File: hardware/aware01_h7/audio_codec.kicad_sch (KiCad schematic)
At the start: 6 parts, among them IC2 TLV320AIC3204IRHBR

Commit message: update pcb
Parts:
- added C60: 100n, Capacitor_SMD:C_0603_1608Metric, symbol Device:C
- C38, C40, C41: Manufacturer_Name (none) -> Murata Electronics; Manufacturer_Part_Number (none) -> GRM188R61E106KA73D; Mouser Part Number (none) -> 81-GRM188R61E106KA3D
- C39, C42: Manufacturer_Name (none) -> KYOCERA AVX; Manufacturer_Part_Number (none) -> KAF15BR72A104KT; Mouser Part Number (none) -> 581-KAF15BR72A104KT
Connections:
- net +3.3VA: now also C60.1
- net GND: now also C60.2

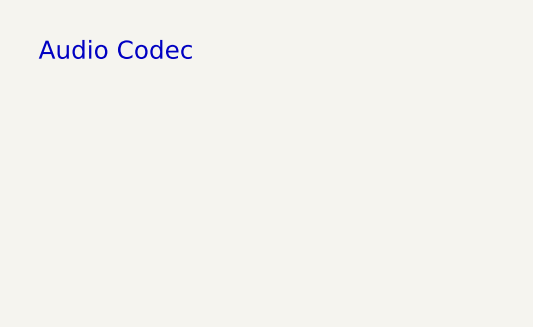
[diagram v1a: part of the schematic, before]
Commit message: change PWR to GND plane and reroute 3V3
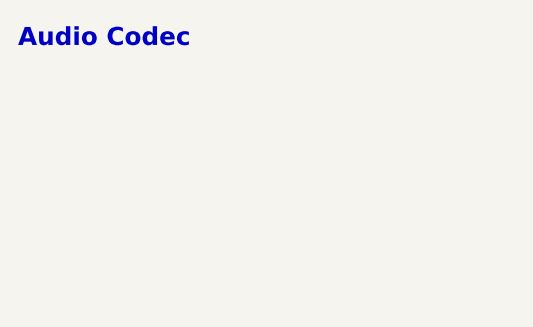
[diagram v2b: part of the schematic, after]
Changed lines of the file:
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@@
 	(text "Audio Codec"
 		(exclude_from_sim no)
-		(at 19.05 18.288 0)
+		(at 16.764 16.764 0)
 		(effects
 			(font
 				(size 2 2)
+				(thickness 0.4)
+				(bold yes)
 			)
 			(justify left top)

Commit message: update to rev 1.2
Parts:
- added C64: 100n, Capacitor_SMD:C_0603_1608Metric, symbol Device:C
- C38: value 10u -> 100n; Manufacturer_Name Murata Electronics -> KYOCERA AVX; Manufacturer_Part_Number GRM188R61E106KA73D -> KAF15BR72A104KT; Mouser Part Number 81-GRM188R61E106KA3D -> 581-KAF15BR72A104KT
- C40, C41: Manufacturer_Name Murata Electronics -> Murata Electronics
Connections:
- net +3.3V: now also C64.2
- net GND: now also C64.1
- net CODECREF: no longer names the net of C41.2, IC2.18 (REF)
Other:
- moved on the sheet: C41

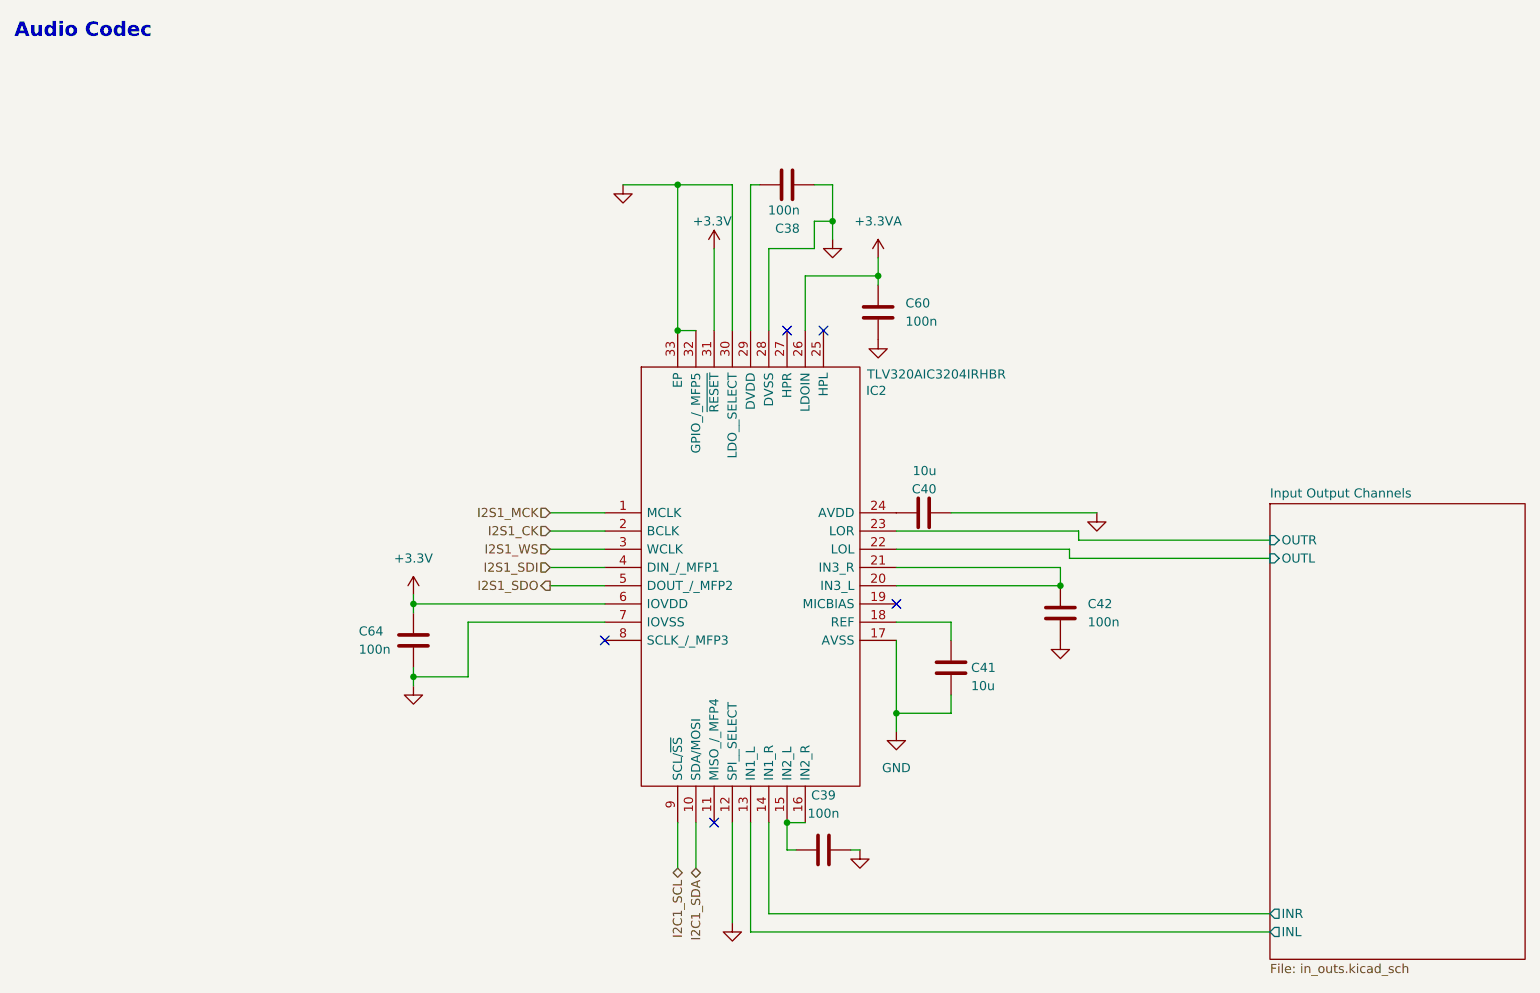
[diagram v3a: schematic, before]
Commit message: rework layout and insert eletrolytic caps for gainstages
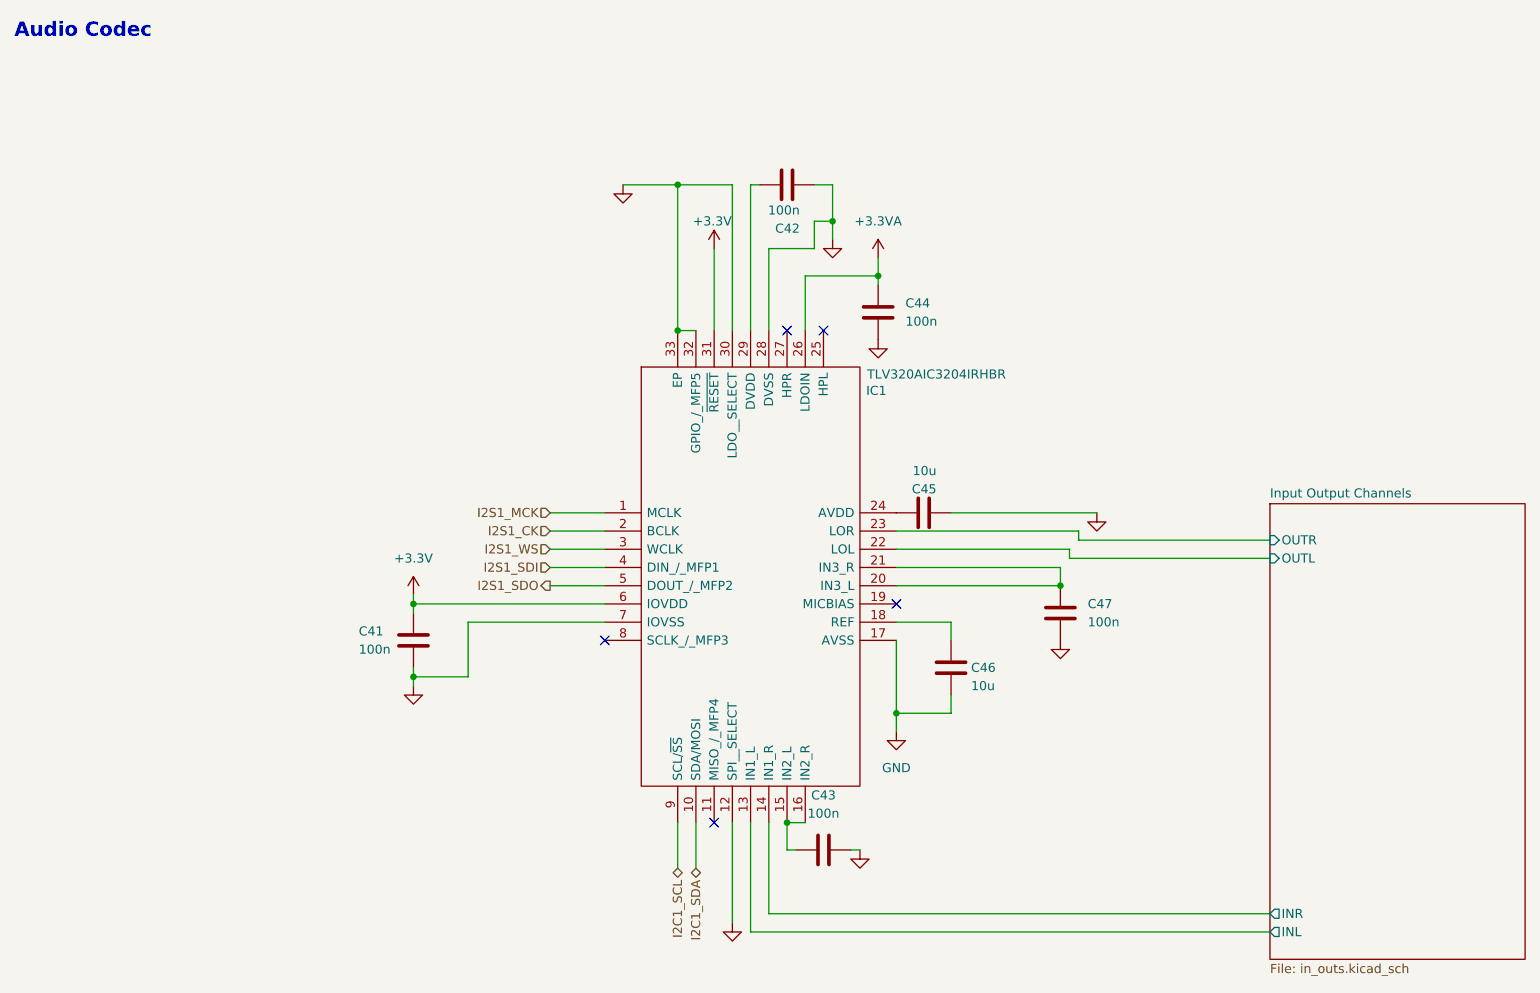
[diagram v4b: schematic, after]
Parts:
- renumbered C64 to C41, C38 to C42, C39 to C43, C60 to C44, C40 to C45, C41 to C46, C42 to C47, IC2 to IC1
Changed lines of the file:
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@@
 		(on_board yes)
 		(dnp no)
-		(property "Reference" "#PWR061"
+		(property "Reference" "#PWR067"
 			(at 167.64 91.44 0)
 			(effects
@@
 			(project "ima_new_codec"
 				(path "/efd43d7c-3c18-45dd-8fa5-4bf32165850f/50dd69da-5058-483c-924f-252f04b072bd"
-					(reference "#PWR061")
+					(reference "#PWR067")
 					(unit 1)
 				)
@@
 		(dnp no)
 		(fields_autoplaced yes)
-		(property "Reference" "#PWR0105"
+		(property "Reference" "#PWR064"
 			(at 137.16 67.31 0)
 			(effects
@@
 			(project "aware01_h7"
 				(path "/efd43d7c-3c18-45dd-8fa5-4bf32165850f/50dd69da-5058-483c-924f-252f04b072bd"
-					(reference "#PWR0105")
+					(reference "#PWR064")
 					(unit 1)
 				)
@@
 		(on_board yes)
 		(dnp no)
-		(property "Reference" "#PWR053"
+		(property "Reference" "#PWR059"
 			(at 114.3 52.07 0)
 			(effects
@@
 			(project "ima_new_codec"
 				(path "/efd43d7c-3c18-45dd-8fa5-4bf32165850f/50dd69da-5058-483c-924f-252f04b072bd"
-					(reference "#PWR053")
+					(reference "#PWR059")
 					(unit 1)
 				)
@@
 		(dnp no)
 		(fields_autoplaced yes)
-		(property "Reference" "#PWR056"
+		(property "Reference" "#PWR062"
 			(at 134.62 138.43 0)
 			(effects
@@
 			(project "ima_new_codec"
 				(path "/efd43d7c-3c18-45dd-8fa5-4bf32165850f/50dd69da-5058-483c-924f-252f04b072bd"
-					(reference "#PWR056")
+					(reference "#PWR062")
 					(unit 1)
 				)
@@
 		(on_board yes)
 		(dnp no)
-		(property "Reference" "C41"
+		(property "Reference" "C46"
 			(at 150.114 106.68 0)
 			(effects
@@
 			(project "ima_new_codec"
 				(path "/efd43d7c-3c18-45dd-8fa5-4bf32165850f/50dd69da-5058-483c-924f-252f04b072bd"
-					(reference "C41")
+					(reference "C46")
 					(unit 1)
 				)
@@
 		(on_board yes)
 		(dnp no)
-		(property "Reference" "C38"
+		(property "Reference" "C42"
 			(at 126.238 45.466 90)
 			(effects
@@
 			(project "ima_new_codec"
 				(path "/efd43d7c-3c18-45dd-8fa5-4bf32165850f/50dd69da-5058-483c-924f-252f04b072bd"
-					(reference "C38")
+					(reference "C42")
 					(unit 1)
 				)
@@
 		(on_board yes)
 		(dnp no)
-		(property "Reference" "C40"
+		(property "Reference" "C45"
 			(at 145.288 81.788 90)
 			(effects
@@
 			(project "ima_new_codec"
 				(path "/efd43d7c-3c18-45dd-8fa5-4bf32165850f/50dd69da-5058-483c-924f-252f04b072bd"
-					(reference "C40")
+					(reference "C45")
 					(unit 1)
 				)
@@
 		(on_board yes)
 		(dnp no)
-		(property "Reference" "C64"
+		(property "Reference" "C41"
 			(at 64.77 101.6 0)
 			(effects
@@
 			(project "aware01_h7_rev1_2"
 				(path "/efd43d7c-3c18-45dd-8fa5-4bf32165850f/50dd69da-5058-483c-924f-252f04b072bd"
-					(reference "C64")
+					(reference "C41")
 					(unit 1)
 				)
@@
 		(dnp no)
 		(fields_autoplaced yes)
-		(property "Reference" "#PWR060"
+		(property "Reference" "#PWR066"
 			(at 162.56 109.22 0)
 			(effects
@@
 			(project "ima_new_codec"
 				(path "/efd43d7c-3c18-45dd-8fa5-4bf32165850f/50dd69da-5058-483c-924f-252f04b072bd"
-					(reference "#PWR060")
+					(reference "#PWR066")
 					(unit 1)
 				)
@@
 		(on_board yes)
 		(dnp no)
-		(property "Reference" "IC2"
+		(property "Reference" "IC1"
 			(at 136.906 68.072 0)
 			(effects
@@
 			(project ""
 				(path "/efd43d7c-3c18-45dd-8fa5-4bf32165850f/50dd69da-5058-483c-924f-252f04b072bd"
-					(reference "IC2")
+					(reference "IC1")
 					(unit 1)
 				)
@@
 		(dnp no)
 		(fields_autoplaced yes)
-		(property "Reference" "C42"
+		(property "Reference" "C47"
 			(at 166.37 97.7899 0)
 			(effects
@@
 			(project "ima_new_codec"
 				(path "/efd43d7c-3c18-45dd-8fa5-4bf32165850f/50dd69da-5058-483c-924f-252f04b072bd"
-					(reference "C42")
+					(reference "C47")
 					(unit 1)
 				)
@@
 		(dnp no)
 		(fields_autoplaced yes)
-		(property "Reference" "#PWR050"
+		(property "Reference" "#PWR056"
 			(at 72.39 100.33 0)
 			(effects
@@
 			(project "ima_new_codec"
 				(path "/efd43d7c-3c18-45dd-8fa5-4bf32165850f/50dd69da-5058-483c-924f-252f04b072bd"
-					(reference "#PWR050")
+					(reference "#PWR056")
 					(unit 1)
 				)
@@
 		(dnp no)
 		(fields_autoplaced yes)
-		(property "Reference" "#PWR052"
+		(property "Reference" "#PWR058"
 			(at 101.6 45.72 0)
 			(effects
@@
 			(project "aware01_h7"
 				(path "/efd43d7c-3c18-45dd-8fa5-4bf32165850f/50dd69da-5058-483c-924f-252f04b072bd"
-					(reference "#PWR052")
+					(reference "#PWR058")
 					(unit 1)
 				)
@@
 		(dnp no)
 		(fields_autoplaced yes)
-		(property "Reference" "#PWR055"
+		(property "Reference" "#PWR061"
 			(at 130.81 53.34 0)
 			(effects
@@
 			(project "ima_new_codec"
 				(path "/efd43d7c-3c18-45dd-8fa5-4bf32165850f/50dd69da-5058-483c-924f-252f04b072bd"
-					(reference "#PWR055")
+					(reference "#PWR061")
 					(unit 1)
 				)
@@
 		(dnp no)
 		(fields_autoplaced yes)
-		(property "Reference" "#PWR051"
+		(property "Reference" "#PWR057"
 			(at 72.39 115.57 0)
 			(effects
@@
 			(project "ima_new_codec"
 				(path "/efd43d7c-3c18-45dd-8fa5-4bf32165850f/50dd69da-5058-483c-924f-252f04b072bd"
-					(reference "#PWR051")
+					(reference "#PWR057")
 					(unit 1)
 				)
@@
 		(dnp no)
 		(fields_autoplaced yes)
-		(property "Reference" "C39"
+		(property "Reference" "C43"
 			(at 129.54 124.46 90)
 			(effects
@@
 			(project "ima_new_codec"
 				(path "/efd43d7c-3c18-45dd-8fa5-4bf32165850f/50dd69da-5058-483c-924f-252f04b072bd"
-					(reference "C39")
+					(reference "C43")
 					(unit 1)
 				)
@@
 		(dnp no)
 		(fields_autoplaced yes)
-		(property "Reference" "#PWR058"
+		(property "Reference" "#PWR065"
 			(at 139.7 121.92 0)
 			(effects
@@
 			(project "ima_new_codec"
 				(path "/efd43d7c-3c18-45dd-8fa5-4bf32165850f/50dd69da-5058-483c-924f-252f04b072bd"
-					(reference "#PWR058")
+					(reference "#PWR065")
 					(unit 1)
 				)
@@
 		(dnp no)
 		(fields_autoplaced yes)
-		(property "Reference" "#PWR057"
+		(property "Reference" "#PWR063"
 			(at 137.16 53.34 0)
 			(effects
@@
 			(project "ima_new_codec"
 				(path "/efd43d7c-3c18-45dd-8fa5-4bf32165850f/50dd69da-5058-483c-924f-252f04b072bd"
-					(reference "#PWR057")
+					(reference "#PWR063")
 					(unit 1)
 				)
@@
 		(dnp no)
 		(fields_autoplaced yes)
-		(property "Reference" "#PWR054"
+		(property "Reference" "#PWR060"
 			(at 116.84 148.59 0)
 			(effects
@@
 			(project "ima_new_codec"
 				(path "/efd43d7c-3c18-45dd-8fa5-4bf32165850f/50dd69da-5058-483c-924f-252f04b072bd"
-					(reference "#PWR054")
+					(reference "#PWR060")
 					(unit 1)
 				)
@@
 		(dnp no)
 		(fields_autoplaced yes)
-		(property "Reference" "C60"
+		(property "Reference" "C44"
 			(at 140.97 55.8799 0)
 			(effects
@@
 			(project ""
 				(path "/efd43d7c-3c18-45dd-8fa5-4bf32165850f/50dd69da-5058-483c-924f-252f04b072bd"
-					(reference "C60")
-					(unit 1)
-				)
+					(reference "C44")
+					(unit 1)
+				)
